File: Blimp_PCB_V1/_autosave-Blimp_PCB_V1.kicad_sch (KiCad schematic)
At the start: 13 parts, among them J1 S8B-PH-K-S

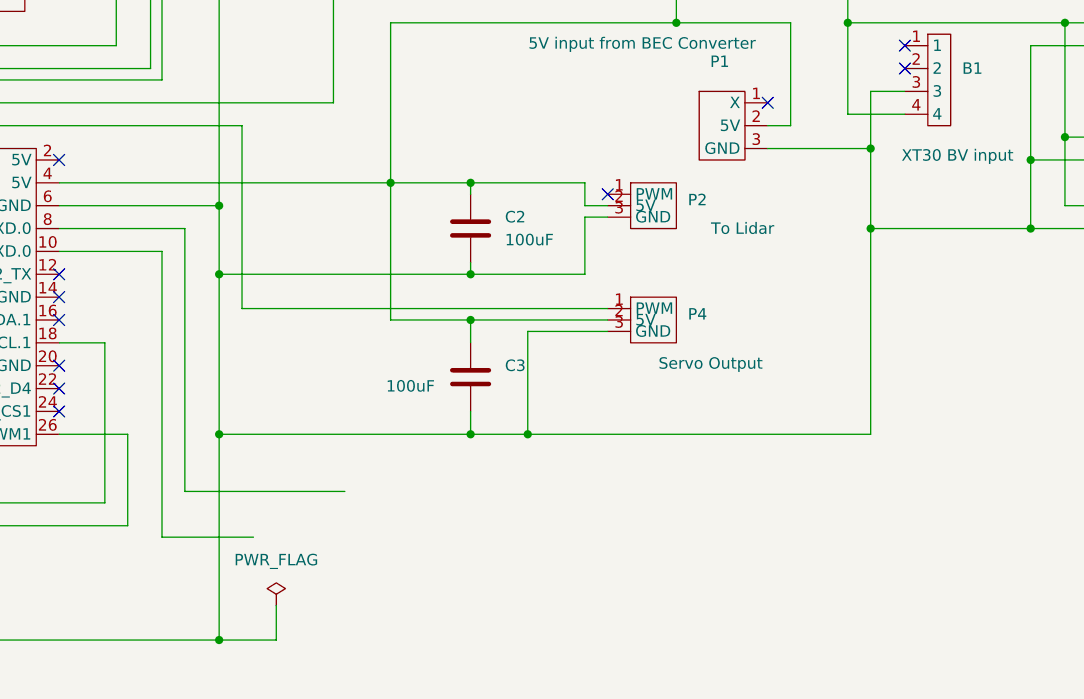
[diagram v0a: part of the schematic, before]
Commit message: Added proper JST Connector for Lidar, Footprint and Symbol
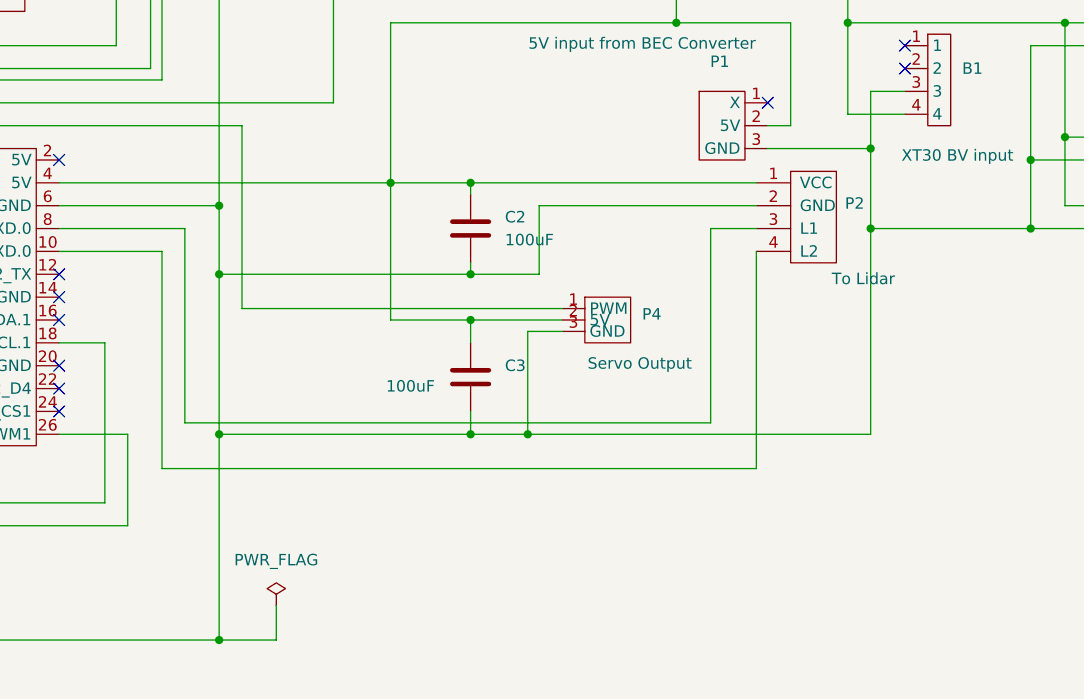
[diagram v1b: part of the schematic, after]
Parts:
- removed P2: ~, PINS:PWM, symbol PWM:PWM
- added P2: ~, JST Connector:JST_XH_B4B-XH-A_1x04_P2.50mm_Vertical, symbol Connector:Conn_01x04_Pin
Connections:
- net +5V: now also P2.1 (VCC)
- net GND: now also P2.2 (GND)
- net at P8.10 (TXD.0): now also P2.4 (L2)
- net at P8.8 (RXD.0): now also P2.3 (L1)
- no-connect marks 35 -> 34
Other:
- moved on the sheet: P4
